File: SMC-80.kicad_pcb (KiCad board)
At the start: 4 copper layers, 101.6 x 102.1 mm, 104 parts, among them J1 RC80 Bus, J10 USB_B_Micro, J2 RC80 Expansion, J3 JTAG, J4 PMOD, J5 PIO Header, J6 Port A, J7 Port A, J8 IDE, J9 Jack-DC, SW1 Reset, SW2 User PB, SW3 User DIP, U1 DS1813R-5+T&R, U10 Z84C0010AEG, U11 SST39SF040, U12 MAX40203AUK, U13 MAX40203AUK, U2 74LVC1G04, U3 EPM7064STC100, U4 LP2985-3.3, U5 TXS0108EPW, U6 Z84C2010AEG, U7 Z84C4310AEG, U8 Z84C3010AEG, U9 AS6C4008A-55ZIN, X1 CFPS-72 50mhz

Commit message: Renamed to SMC-80
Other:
- board text added: "SMC-80 Model I"
- board text removed: "THS-80 Model I"
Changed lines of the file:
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@@
   (page A4)
   (title_block
-    (title THS-80)
+    (title SMC-80)
     (date 2019-08-13)
     (rev 1.0)
@@
     (effects (font (size 0.8128 0.8128) (thickness 0.1524)))
   )
-  (gr_text "THS-80 Model I" (at 161.544 98.552) (layer F.SilkS)
+  (gr_text "SMC-80 Model I" (at 161.544 98.552) (layer F.SilkS)
     (effects (font (size 1.8288 1.8288) (thickness 0.4064)))
   )

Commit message: trace routing
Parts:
- added U14: AZ2940-5.0, Package_TO_SOT_SMD:TO-252-2, F.Cu at (140.0, 125.7)
- moved U13 10.4 mm to (146.3, 129.5)
- moved C35 6.37 mm to (147.1, 126.7), turned to 180 degrees
- moved D11 6.35 mm to (147.1, 121.7)
- moved R20 6.35 mm to (147.1, 123.7)
- moved C23 5.21 mm to (142.1, 44.6), turned to 0 degrees
- moved C31 2.30 mm to (133.6, 124.0)
- moved C33 2.30 mm to (133.6, 126.0)
- moved C29 2.30 mm to (133.6, 121.4)
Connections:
- J1 pad 10: (no net) -> Net-(J1-Pad10)
- J1 pad 12: (no net) -> Net-(J1-Pad12)
- J1 pad 14: (no net) -> Net-(J1-Pad14)
- J1 pad 16: (no net) -> Net-(J1-Pad16)
- J1 pad 18: (no net) -> Net-(J1-Pad18)
- J1 pad 2: (no net) -> Net-(J1-Pad2)
- J1 pad 20: (no net) -> Net-(J1-Pad20)
- J1 pad 22: (no net) -> Net-(J1-Pad22)
- J1 pad 24: (no net) -> Net-(J1-Pad24)
- J1 pad 26: (no net) -> Net-(J1-Pad26)
- J1 pad 28: /A18 -> Net-(J1-Pad28)
- J1 pad 30: /A17 -> Net-(J1-Pad30)
- J1 pad 32: /A16 -> Net-(J1-Pad32)
- J1 pad 4: (no net) -> Net-(J1-Pad4)
- J1 pad 54: (no net) -> Net-(J1-Pad54)
- J1 pad 56: (no net) -> Net-(J1-Pad56)
- J1 pad 58: (no net) -> Net-(J1-Pad58)
- J1 pad 6: (no net) -> Net-(J1-Pad6)
- J1 pad 60: (no net) -> Net-(J1-Pad60)
- J1 pad 62: (no net) -> Net-(J1-Pad62)
- J1 pad 64: (no net) -> Net-(J1-Pad64)
- J1 pad 66: (no net) -> Net-(J1-Pad66)
- J1 pad 68: (no net) -> Net-(J1-Pad68)
- J1 pad 73: (no net) -> Net-(J1-Pad73)
- J1 pad 74: (no net) -> Net-(J1-Pad74)
- J1 pad 75: (no net) -> Net-(J1-Pad75)
- J1 pad 76: (no net) -> Net-(J1-Pad76)
- J1 pad 77: (no net) -> Net-(J1-Pad77)
- J1 pad 78: (no net) -> Net-(J1-Pad78)
- J1 pad 8: (no net) -> Net-(J1-Pad8)
- J10 pad 2: (no net) -> Net-(J10-Pad2)
- J10 pad 3: (no net) -> Net-(J10-Pad3)
- J2 pad 10: (no net) -> Net-(J2-Pad10)
- J2 pad 12: (no net) -> Net-(J2-Pad12)
- J2 pad 14: (no net) -> Net-(J2-Pad14)
- J2 pad 16: (no net) -> Net-(J2-Pad16)
- J2 pad 18: (no net) -> Net-(J2-Pad18)
- J2 pad 2: (no net) -> Net-(J2-Pad2)
- J2 pad 20: (no net) -> Net-(J2-Pad20)
- J2 pad 22: (no net) -> Net-(J2-Pad22)
- J2 pad 24: (no net) -> Net-(J2-Pad24)
- J2 pad 26: (no net) -> Net-(J2-Pad26)
- J2 pad 28: /A18 -> Net-(J2-Pad28)
- J2 pad 30: /A17 -> Net-(J2-Pad30)
- J2 pad 32: /A16 -> Net-(J2-Pad32)
- J2 pad 4: (no net) -> Net-(J2-Pad4)
- J2 pad 54: (no net) -> Net-(J2-Pad54)
- J2 pad 56: (no net) -> Net-(J2-Pad56)
- J2 pad 58: (no net) -> Net-(J2-Pad58)
- J2 pad 6: (no net) -> Net-(J2-Pad6)
- J2 pad 60: (no net) -> Net-(J2-Pad60)
- J2 pad 62: (no net) -> Net-(J2-Pad62)
- J2 pad 64: (no net) -> Net-(J2-Pad64)
- J2 pad 66: (no net) -> Net-(J2-Pad66)
- J2 pad 68: (no net) -> Net-(J2-Pad68)
- J2 pad 73: (no net) -> Net-(J2-Pad73)
- J2 pad 74: (no net) -> Net-(J2-Pad74)
- J2 pad 75: (no net) -> Net-(J2-Pad75)
- J2 pad 76: (no net) -> Net-(J2-Pad76)
- J2 pad 77: (no net) -> Net-(J2-Pad77)
- J2 pad 78: (no net) -> Net-(J2-Pad78)
- J2 pad 8: (no net) -> Net-(J2-Pad8)
- J3 pad 6: (no net) -> Net-(J3-Pad6)
- J3 pad 7: (no net) -> Net-(J3-Pad7)
- J3 pad 8: (no net) -> Net-(J3-Pad8)
- J8 pad 10: (no net) -> Net-(J8-Pad10)
- J8 pad 12: (no net) -> Net-(J8-Pad12)
- J8 pad 14: (no net) -> Net-(J8-Pad14)
- J8 pad 16: (no net) -> Net-(J8-Pad16)
- J8 pad 18: (no net) -> Net-(J8-Pad18)
- J8 pad 21: (no net) -> Net-(J8-Pad21)
- J8 pad 27: (no net) -> Net-(J8-Pad27)
- J8 pad 28: (no net) -> Net-(J8-Pad28)
- J8 pad 31: (no net) -> Net-(J8-Pad31)
- J8 pad 32: (no net) -> Net-(J8-Pad32)
- J8 pad 4: (no net) -> Net-(J8-Pad4)
- J8 pad 6: (no net) -> Net-(J8-Pad6)
- J8 pad 8: (no net) -> Net-(J8-Pad8)
- U10 pad 11: (no net) -> Net-(U10-Pad11)
- U10 pad 17: (no net) -> Net-(U10-Pad17)
- U10 pad 33: (no net) -> Net-(U10-Pad33)
- U10 pad 39: (no net) -> Net-(U10-Pad39)
- U12 pad 4: (no net) -> Net-(U12-Pad4)
- U13 pad 1: Net-(C29-Pad1) -> Net-(U13-Pad1)
- U13 pad 3: Net-(C29-Pad1) -> Net-(U13-Pad1)
- U13 pad 4: (no net) -> Net-(U13-Pad4)
- U3 pad 1: (no net) -> Net-(U3-Pad1)
- U3 pad 13: /CPLD/SW3 -> /CPLD/SW0
- U3 pad 14: /CPLD/SW2 -> /CPLD/SW1
- U3 pad 16: /CPLD/SW1 -> /CPLD/SW2
- U3 pad 17: /CPLD/SW0 -> /CPLD/SW3
- U3 pad 2: (no net) -> Net-(U3-Pad2)
- U3 pad 22: (no net) -> Net-(U3-Pad22)
- U3 pad 24: (no net) -> Net-(U3-Pad24)
- U3 pad 27: (no net) -> Net-(U3-Pad27)
- U3 pad 28: (no net) -> Net-(U3-Pad28)
- U3 pad 49: (no net) -> Net-(U3-Pad49)
- U3 pad 5: (no net) -> Net-(U3-Pad5)
- U3 pad 50: (no net) -> Net-(U3-Pad50)
- U3 pad 53: (no net) -> Net-(U3-Pad53)
- U3 pad 55: (no net) -> Net-(U3-Pad55)
- U3 pad 7: (no net) -> Net-(U3-Pad7)
- U3 pad 70: (no net) -> Net-(U3-Pad70)
- U3 pad 72: (no net) -> Net-(U3-Pad72)
- U3 pad 77: (no net) -> Net-(U3-Pad77)
- U3 pad 78: (no net) -> Net-(U3-Pad78)
- U3 pad 90: (no net) -> Net-(U3-Pad90)
- U6 pad 2: (no net) -> Net-(U6-Pad2)
- U6 pad 28: (no net) -> Net-(U6-Pad28)
- U6 pad 39: (no net) -> Net-(U6-Pad39)
- U7 pad 1: (no net) -> Net-(U7-Pad1)
- U7 pad 10: (no net) -> Net-(U7-Pad10)
- U7 pad 15: (no net) -> Net-(U7-Pad15)
- U7 pad 16: (no net) -> Net-(U7-Pad16)
- U7 pad 17: (no net) -> Net-(U7-Pad17)
- U7 pad 28: (no net) -> Net-(U7-Pad28)
- U7 pad 38: (no net) -> Net-(U7-Pad38)
- U7 pad 39: (no net) -> Net-(U7-Pad39)
- U7 pad 40: (no net) -> Net-(U7-Pad40)
- U8 pad 11: (no net) -> Net-(U8-Pad11)
- U8 pad 15: (no net) -> Net-(U8-Pad15)
- U8 pad 17: (no net) -> Net-(U8-Pad17)
- U8 pad 20: (no net) -> Net-(U8-Pad20)
- U8 pad 24: (no net) -> Net-(U8-Pad24)
- U8 pad 26: (no net) -> Net-(U8-Pad26)
- U8 pad 28: (no net) -> Net-(U8-Pad28)
- U8 pad 30: (no net) -> Net-(U8-Pad30)
- U8 pad 34: (no net) -> Net-(U8-Pad34)
- U8 pad 38: (no net) -> Net-(U8-Pad38)
- U8 pad 39: (no net) -> Net-(U8-Pad39)
- U8 pad 42: (no net) -> Net-(U8-Pad42)
- U8 pad 44: (no net) -> Net-(U8-Pad44)
- U8 pad 5: (no net) -> Net-(U8-Pad5)
- U8 pad 6: (no net) -> Net-(U8-Pad6)
- U8 pad 7: (no net) -> Net-(U8-Pad7)
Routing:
- net /~RD: track 87.9 -> 229.4 mm, vias 4 -> 11
- net /~WR: track 8.62 -> 132.0 mm, vias 0 -> 7
- net /D0: track 124.6 -> 202.6 mm, vias 5 -> 9
- net /D1: track 123.7 -> 201.5 mm, vias 5 -> 11
- net /D4: track 163.3 -> 237.7 mm, vias 11 -> 12
- net /D2: track 95.4 -> 167.7 mm, vias 4 -> 8
- net /D3: track 162.0 -> 233.1 mm, vias 11 -> 13
- net /D7: track 80.7 -> 151.2 mm, vias 4 -> 7
- net /CPLD/MA17: track 68.5 -> 0.00 mm, vias 6 -> 0
- net /D5: track 153.7 -> 221.4 mm, vias 11 -> 14
- net /CPLD/MA18: track 65.5 -> 0.00 mm, vias 2 -> 0
- net /A15: track 8.62 -> 73.7 mm, vias 0 -> 2
- net /A2: track 57.7 -> 120.7 mm, vias 1 -> 2
- net /A7: track 34.3 -> 96.2 mm, vias 0 -> 2
- net /A14: track 8.62 -> 69.8 mm, vias 0 -> 2
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
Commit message: Routing finished
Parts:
- removed the C13 at (112.0, 72.1)
- removed the C14 at (108.2, 73.7)
- removed the C16 at (104.9, 73.7)
- removed the C17 at (115.8, 73.9)
- removed the C18 at (114.6, 80.5)
- removed the C19 at (119.1, 80.5)
- removed the J4 at (108.0, 76.5)
- removed the JP1 at (113.0, 54.6)
- removed the R1 at (113.0, 62.7)
- removed the R7 at (114.6, 89.7)
- removed the RN4 at (111.4, 85.1)
- removed the SW1 at (104.1, 54.6)
- removed the U4 at (111.9, 74.9)
- removed the U5 at (116.8, 85.1)
- added C11: 100nF, Capacitor_SMD:C_0603_1608Metric_Pad1.05x0.95mm_HandSolder, F.Cu at (114.6, 80.5)
- added C2: 100nF, Capacitor_SMD:C_0603_1608Metric_Pad1.05x0.95mm_HandSolder, F.Cu at (108.2, 73.9)
- added C31: 1uF, Capacitor_SMD:C_0603_1608Metric_Pad1.05x0.95mm_HandSolder, F.Cu at (112.0, 72.1)
- added C32: 10nF, Capacitor_SMD:C_0603_1608Metric_Pad1.05x0.95mm_HandSolder, F.Cu at (115.8, 75.9)
- added C35: 1uF, Capacitor_SMD:C_0603_1608Metric_Pad1.05x0.95mm_HandSolder, F.Cu at (115.8, 73.9)
- added C5: 100nF, Capacitor_SMD:C_0603_1608Metric_Pad1.05x0.95mm_HandSolder, F.Cu at (104.6, 73.9)
- added D11: Green, LED_SMD:LED_0603_1608Metric_Pad1.05x0.95mm_HandSolder, F.Cu at (115.8, 69.6)
- added J3: PMOD, Connector_PinSocket_2.54mm:PinSocket_2x06_P2.54mm_Horizontal_Top_Bottom, F.Cu at (107.7, 76.7)
- added JP5: Reset Ena, Connector_PinHeader_2.54mm:PinHeader_1x03_P2.54mm_Vertical, F.Cu at (113.0, 54.6)
- added R19: 360R, Resistor_SMD:R_0603_1608Metric_Pad1.05x0.95mm_HandSolder, F.Cu at (115.8, 67.8)
- added R21: 10K, Resistor_SMD:R_0603_1608Metric_Pad1.05x0.95mm_HandSolder, F.Cu at (113.0, 62.7)
- added R3: 1K, Resistor_SMD:R_0603_1608Metric_Pad1.05x0.95mm_HandSolder, F.Cu at (114.6, 89.7)
- added RN3: 200R, Resistor_SMD:R_Cat16-8, F.Cu at (111.3, 85.1)
- added SW3: Reset, Button_Switch_SMD:SW_SPST_FSMSM, F.Cu at (104.1, 54.4)
- added U12: LP2985-3.3, Package_TO_SOT_SMD:SOT-23-5, F.Cu at (112.0, 74.9)
- added U14: DS1813R-5+T&R, Package_TO_SOT_SMD:SOT-23, F.Cu at (108.5, 58.9)
- C15: value 10nF -> 100nF
- U1: value DS1813R-5+T&R -> TXS0108EPW; footprint Package_TO_SOT_SMD:SOT-23 -> Package_SO:TSSOP-20_4.4x6.5mm_P0.65mm
- moved U1 27.5 mm to (116.8, 85.1)
- moved C15 5.64 mm to (119.1, 80.5)
- renumbered C7 to C10, C9 to C12, C10 to C13, C11 to C14, C12 to C16, C20 to C17, C21 to C18, C22 to C19, C23 to C20, C24 to C21, C25 to C22, C26 to C23, C27 to C24, C29 to C25, C28 to C26, C31 to C27, C30 to C28, C33 to C29, C4 to C3, C32 to C30, C35 to C33, C2 to C4, C3 to C6, C5 to C7, C6 to C8, C8 to C9, D11 to D12, J3 to J4, JP2 to JP1, JP3 to JP2, JP4 to JP3, JP5 to JP4, R2 to R1, R11 to R10, R12 to R11, R13 to R12, R14 to R13, R15 to R14, R16 to R15, R17 to R16, R18 to R17, R19 to R18, R3 to R2, R8 to R7, R9 to R8, R10 to R9, RN3 to RN4, SW3 to SW1, U14 to U10, U13 to U11, U12 to U13, U6 to U4, U7 to U5, U8 to U6, U9 to U7, U10 to U8, U11 to U9
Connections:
- C15 pad 1: Net-(C15-Pad1) -> VCC
- J1 pad 10: Net-(J1-Pad10) -> (no net)
- J1 pad 12: Net-(J1-Pad12) -> (no net)
- J1 pad 14: Net-(J1-Pad14) -> (no net)
- J1 pad 16: Net-(J1-Pad16) -> (no net)
- J1 pad 18: Net-(J1-Pad18) -> (no net)
- J1 pad 2: Net-(J1-Pad2) -> (no net)
- J1 pad 20: Net-(J1-Pad20) -> (no net)
- J1 pad 22: Net-(J1-Pad22) -> (no net)
- J1 pad 24: Net-(J1-Pad24) -> (no net)
- J1 pad 26: Net-(J1-Pad26) -> (no net)
- J1 pad 28: Net-(J1-Pad28) -> (no net)
- J1 pad 30: Net-(J1-Pad30) -> (no net)
- J1 pad 32: Net-(J1-Pad32) -> (no net)
- J1 pad 4: Net-(J1-Pad4) -> (no net)
- J1 pad 54: Net-(J1-Pad54) -> (no net)
- J1 pad 56: Net-(J1-Pad56) -> (no net)
- J1 pad 58: Net-(J1-Pad58) -> (no net)
- J1 pad 6: Net-(J1-Pad6) -> (no net)
- J1 pad 60: Net-(J1-Pad60) -> (no net)
- J1 pad 62: Net-(J1-Pad62) -> (no net)
- J1 pad 64: Net-(J1-Pad64) -> (no net)
- J1 pad 66: Net-(J1-Pad66) -> (no net)
- J1 pad 68: Net-(J1-Pad68) -> (no net)
- J1 pad 73: Net-(J1-Pad73) -> (no net)
- J1 pad 74: Net-(J1-Pad74) -> (no net)
- J1 pad 75: Net-(J1-Pad75) -> (no net)
- J1 pad 76: Net-(J1-Pad76) -> (no net)
- J1 pad 77: Net-(J1-Pad77) -> (no net)
- J1 pad 78: Net-(J1-Pad78) -> (no net)
- J1 pad 8: Net-(J1-Pad8) -> (no net)
- J10 pad 2: Net-(J10-Pad2) -> (no net)
- J10 pad 3: Net-(J10-Pad3) -> (no net)
- J2 pad 10: Net-(J2-Pad10) -> (no net)
- J2 pad 12: Net-(J2-Pad12) -> (no net)
- J2 pad 14: Net-(J2-Pad14) -> (no net)
- J2 pad 16: Net-(J2-Pad16) -> (no net)
- J2 pad 18: Net-(J2-Pad18) -> (no net)
- J2 pad 2: Net-(J2-Pad2) -> (no net)
- J2 pad 20: Net-(J2-Pad20) -> (no net)
- J2 pad 22: Net-(J2-Pad22) -> (no net)
- J2 pad 24: Net-(J2-Pad24) -> (no net)
- J2 pad 26: Net-(J2-Pad26) -> (no net)
- J2 pad 28: Net-(J2-Pad28) -> (no net)
- J2 pad 30: Net-(J2-Pad30) -> (no net)
- J2 pad 32: Net-(J2-Pad32) -> (no net)
- J2 pad 4: Net-(J2-Pad4) -> (no net)
- J2 pad 54: Net-(J2-Pad54) -> (no net)
- J2 pad 56: Net-(J2-Pad56) -> (no net)
- J2 pad 58: Net-(J2-Pad58) -> (no net)
- J2 pad 6: Net-(J2-Pad6) -> (no net)
- J2 pad 60: Net-(J2-Pad60) -> (no net)
- J2 pad 62: Net-(J2-Pad62) -> (no net)
- J2 pad 64: Net-(J2-Pad64) -> (no net)
- J2 pad 66: Net-(J2-Pad66) -> (no net)
- J2 pad 68: Net-(J2-Pad68) -> (no net)
- J2 pad 73: Net-(J2-Pad73) -> (no net)
- J2 pad 74: Net-(J2-Pad74) -> (no net)
- J2 pad 75: Net-(J2-Pad75) -> (no net)
- J2 pad 76: Net-(J2-Pad76) -> (no net)
- J2 pad 77: Net-(J2-Pad77) -> (no net)
- J2 pad 78: Net-(J2-Pad78) -> (no net)
- J2 pad 8: Net-(J2-Pad8) -> (no net)
- J4 pad 6: Net-(J3-Pad6) -> (no net)
- J4 pad 7: Net-(J3-Pad7) -> (no net)
- J4 pad 8: Net-(J3-Pad8) -> (no net)
- J8 pad 10: Net-(J8-Pad10) -> (no net)
- J8 pad 12: Net-(J8-Pad12) -> (no net)
- J8 pad 14: Net-(J8-Pad14) -> (no net)
- J8 pad 16: Net-(J8-Pad16) -> (no net)
- J8 pad 18: Net-(J8-Pad18) -> (no net)
- J8 pad 21: Net-(J8-Pad21) -> (no net)
- J8 pad 27: Net-(J8-Pad27) -> (no net)
- J8 pad 28: Net-(J8-Pad28) -> (no net)
- J8 pad 31: Net-(J8-Pad31) -> (no net)
- J8 pad 32: Net-(J8-Pad32) -> (no net)
- J8 pad 4: Net-(J8-Pad4) -> (no net)
- J8 pad 6: Net-(J8-Pad6) -> (no net)
- J8 pad 8: Net-(J8-Pad8) -> (no net)
- U1 pad 1: /~RST -> Net-(RN3-Pad16)
- U1 pad 2: VCC -> +3V3
- U1 pad 3: GND -> Net-(RN3-Pad15)
- U11 pad 4: Net-(U13-Pad4) -> (no net)
- U13 pad 4: Net-(U12-Pad4) -> (no net)
- U3 pad 1: Net-(U3-Pad1) -> (no net)
- U3 pad 19: /CPLD/PMOD10 -> /CPLD/PMOD1
- U3 pad 2: Net-(U3-Pad2) -> (no net)
- U3 pad 20: /CPLD/PMOD4 -> /CPLD/PMOD7
- U3 pad 21: /CPLD/PMOD9 -> /CPLD/PMOD2
- U3 pad 22: Net-(U3-Pad22) -> (no net)
- U3 pad 23: /CPLD/PMOD3 -> /CPLD/PMOD8
- U3 pad 24: Net-(U3-Pad24) -> (no net)
- U3 pad 25: /CPLD/PMOD8 -> /CPLD/PMOD3
- U3 pad 27: Net-(U3-Pad27) -> (no net)
- U3 pad 28: Net-(U3-Pad28) -> (no net)
- U3 pad 29: /CPLD/PMOD2 -> /CPLD/PMOD9
- U3 pad 30: /CPLD/PMOD7 -> /CPLD/PMOD4
- U3 pad 31: /CPLD/PMOD1 -> /CPLD/PMOD10
- U3 pad 49: Net-(U3-Pad49) -> (no net)
- U3 pad 5: Net-(U3-Pad5) -> (no net)
- U3 pad 50: Net-(U3-Pad50) -> (no net)
- U3 pad 53: Net-(U3-Pad53) -> (no net)
- U3 pad 55: Net-(U3-Pad55) -> (no net)
- U3 pad 7: Net-(U3-Pad7) -> (no net)
- U3 pad 70: Net-(U3-Pad70) -> (no net)
- U3 pad 72: Net-(U3-Pad72) -> (no net)
- U3 pad 77: Net-(U3-Pad77) -> (no net)
- U3 pad 78: Net-(U3-Pad78) -> (no net)
- U3 pad 90: Net-(U3-Pad90) -> (no net)
- U4 pad 2: Net-(U6-Pad2) -> (no net)
- U4 pad 28: Net-(U6-Pad28) -> (no net)
- U4 pad 39: Net-(U6-Pad39) -> (no net)
- U5 pad 1: Net-(U7-Pad1) -> (no net)
- U5 pad 10: Net-(U7-Pad10) -> (no net)
- U5 pad 15: Net-(U7-Pad15) -> (no net)
- U5 pad 16: Net-(U7-Pad16) -> (no net)
- U5 pad 17: Net-(U7-Pad17) -> (no net)
- U5 pad 28: Net-(U7-Pad28) -> (no net)
- U5 pad 38: Net-(U7-Pad38) -> (no net)
- U5 pad 39: Net-(U7-Pad39) -> (no net)
- U5 pad 40: Net-(U7-Pad40) -> (no net)
- U6 pad 11: Net-(U8-Pad11) -> (no net)
- U6 pad 15: Net-(U8-Pad15) -> (no net)
- U6 pad 17: Net-(U8-Pad17) -> (no net)
- U6 pad 20: Net-(U8-Pad20) -> (no net)
- U6 pad 24: Net-(U8-Pad24) -> (no net)
- U6 pad 26: Net-(U8-Pad26) -> (no net)
- U6 pad 28: Net-(U8-Pad28) -> (no net)
- U6 pad 30: Net-(U8-Pad30) -> (no net)
- U6 pad 34: Net-(U8-Pad34) -> (no net)
- U6 pad 38: Net-(U8-Pad38) -> (no net)
- U6 pad 39: Net-(U8-Pad39) -> (no net)
- U6 pad 42: Net-(U8-Pad42) -> (no net)
- U6 pad 44: Net-(U8-Pad44) -> (no net)
- U6 pad 5: Net-(U8-Pad5) -> (no net)
- U6 pad 6: Net-(U8-Pad6) -> (no net)
- U6 pad 7: Net-(U8-Pad7) -> (no net)
- U8 pad 11: Net-(U10-Pad11) -> (no net)
- U8 pad 17: Net-(U10-Pad17) -> (no net)
- U8 pad 33: Net-(U10-Pad33) -> (no net)
- U8 pad 39: Net-(U10-Pad39) -> (no net)
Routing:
- net /D7: track 151.2 -> 268.1 mm, vias 7 -> 12
- net /~RESET: track 99.2 -> 206.7 mm, vias 5 -> 11
- net /D2: track 167.7 -> 266.2 mm, vias 8 -> 13
- net /IEO: track 8.62 -> 92.7 mm, vias 0 -> 2
- net /RXA: track 8.62 -> 77.0 mm, vias 0 -> 5
- net /CPLD/MA17: track 0.00 -> 68.2 mm, vias 0 -> 6
- net /CPLD/MA18: track 0.00 -> 65.2 mm, vias 0 -> 2
- net /TXA: track 8.62 -> 73.2 mm, vias 0 -> 3
- net /~IORQ: track 85.7 -> 147.0 mm, vias 6 -> 9
- net /~INT: track 77.5 -> 136.4 mm, vias 6 -> 9
- net /CPLD/MA16: track 0.00 -> 58.0 mm, vias 0 -> 2
- net /SIO_~CE: track 0.00 -> 55.7 mm, vias 0 -> 6
- net /MA17: track 51.9 -> 0.00 mm, vias 5 -> 0
- net /A1: track 203.5 -> 253.4 mm, vias 9 -> 12
- net /A0: track 196.7 -> 245.0 mm, vias 9 -> 12
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
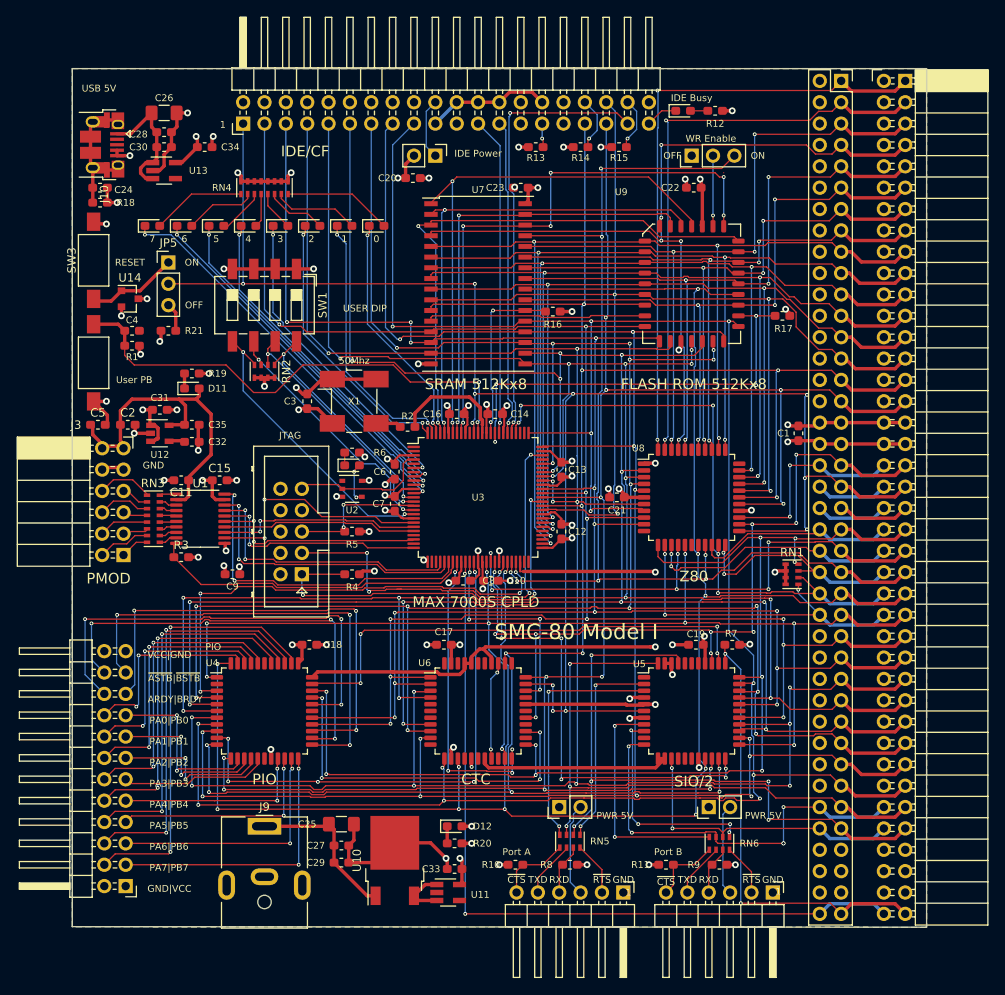
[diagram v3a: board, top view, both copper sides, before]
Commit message: reorganized sheets, added SIO clk select
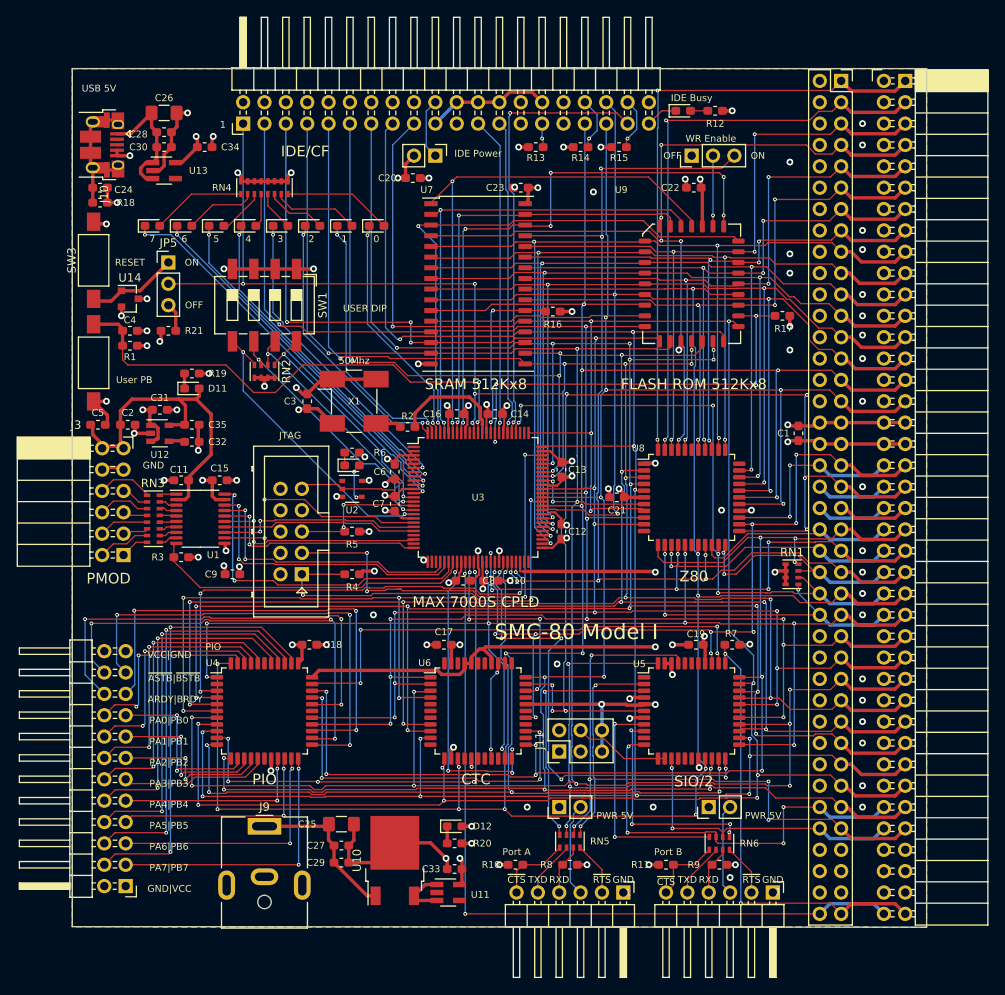
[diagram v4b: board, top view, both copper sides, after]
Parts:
- added J11: SIO CLK SEL, Connector_PinHeader_2.54mm:PinHeader_2x03_P2.54mm_Vertical, F.Cu at (159.5, 112.8)
- moved C4 0.25 mm to (108.5, 62.7)
- moved R1 0.25 mm to (108.5, 64.5)
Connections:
- U6 pad 16: /CLK2 -> /Peripherals/TO_0
- U6 pad 18: /Peripherals/CLK_B -> /Peripherals/TO_1
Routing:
- net /CLK2: track 70.2 -> 38.0 mm, vias 2 -> 1
- net /Peripherals/CLK_B: track 23.5 -> 11.4 mm
- net /CLK: track 141.3 -> 147.1 mm, vias 4 -> 5
- net /D7: track 268.1 -> 266.8 mm
- net /SIO_~CE: track 55.7 -> 57.0 mm
- net /Peripherals/TO_0: track 0.00 -> 1.01 mm, vias 0 -> 1
- net /D6: track 245.7 -> 244.8 mm
- net GND: track 158.6 -> 159.4 mm, vias 52 -> 84
- net /Peripherals/~CTSA: track 29.0 -> 29.6 mm
- net /CPLD/USER_PB: track 59.3 -> 59.9 mm
- net VCC: track 135.8 -> 135.3 mm
- net /Peripherals/~RTSB: track 25.6 -> 26.1 mm
- net /TXB: track 48.9 -> 49.3 mm, vias 5 -> 4

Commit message: remove old files, added jtag pullup
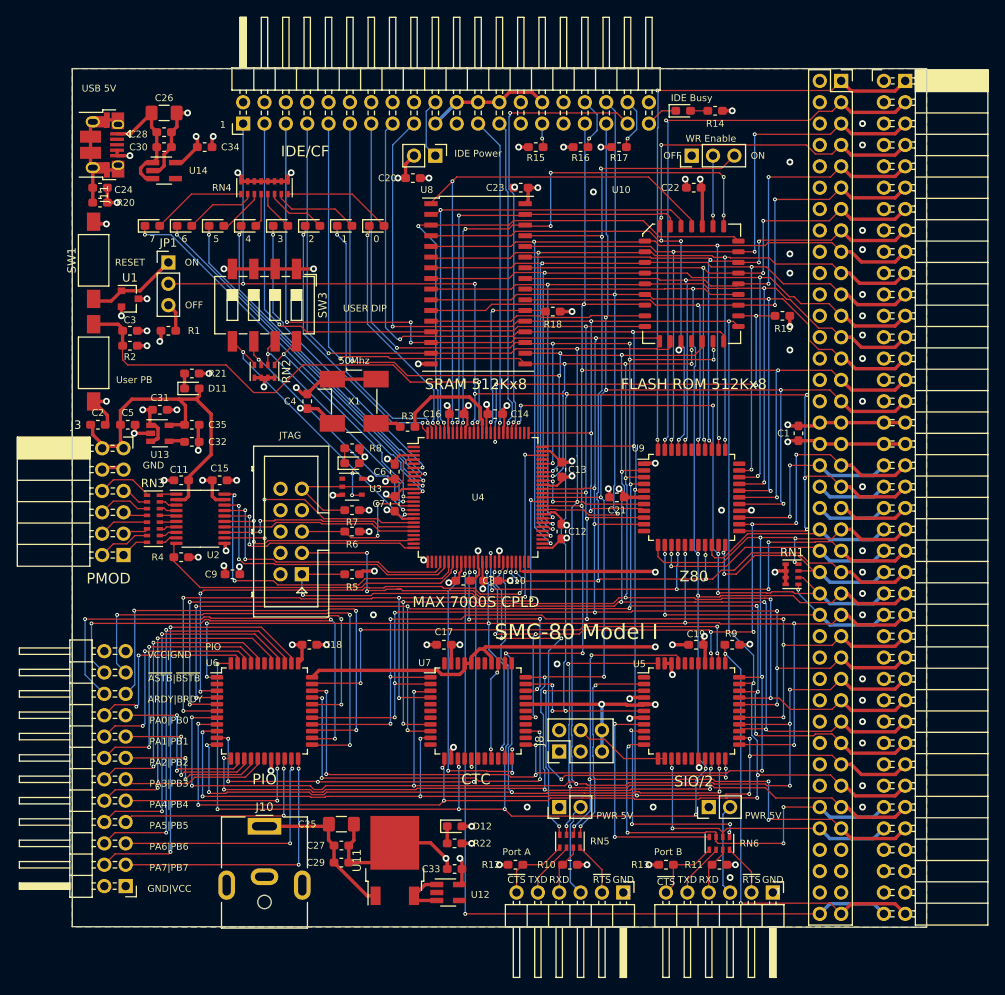
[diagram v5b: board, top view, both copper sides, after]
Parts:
- removed the R6 at (134.9, 77.2)
- removed the U2 at (134.9, 81.5)
- added R7: 10K, Resistor_SMD:R_0603_1608Metric_Pad1.05x0.95mm_HandSolder, F.Cu at (134.9, 84.1)
- added R8: 360R, Resistor_SMD:R_0603_1608Metric_Pad1.05x0.95mm_HandSolder, F.Cu at (134.9, 76.7)
- added U3: 74LVC1G04, Package_SO:TSOP-5_1.65x3.05mm_P0.95mm, F.Cu at (134.9, 81.3)
- moved D9 0.25 mm to (134.9, 78.5)
- renumbered C5 to C2, C4 to C3, C3 to C4, C2 to C5, J9 to J10, J10 to J11, J11 to J8, J8 to J9, JP5 to JP1, JP1 to JP2, JP2 to JP3, JP3 to JP4, JP4 to JP5, R21 to R1, R8 to R10, R9 to R11, R10 to R12, R11 to R13, R12 to R14, R13 to R15, R14 to R16, R15 to R17, R16 to R18, R17 to R19, R1 to R2, R18 to R20, R19 to R21, R20 to R22, R2 to R3, R3 to R4, R4 to R5, R5 to R6, R7 to R9, SW3 to SW1, SW1 to SW3, U14 to U1, U9 to U10, U10 to U11, U11 to U12, U12 to U13, U13 to U14, U1 to U2, U3 to U4, U4 to U6, U6 to U7, U7 to U8, U8 to U9
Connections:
- net /CPLD/OE1 renamed /CPLD/PMOD_ENA
- U6 pad 30: /Peripherals/IEO_1 -> /IEO_2
- U6 pad 32: /Peripherals/IEO_0 -> /Peripherals/IEO_1
- U7 pad 22: /IEO_2 -> /Peripherals/IEO_1
- U7 pad 25: /Peripherals/IEO_1 -> /Peripherals/IEO_0
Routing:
- net /CPLD/TDI: track 16.2 -> 22.1 mm
- net /CPLD/SW3: track 35.1 -> 32.9 mm
- net /CPLD/TMS: track 16.9 -> 18.2 mm
- net VCC: track 135.3 -> 136.5 mm, vias 41 -> 42
